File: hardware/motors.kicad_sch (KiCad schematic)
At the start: 11 parts, among them J2 JST_PH_01x02, J3 JST_XH_01x02, J4 JST_XH_01x02, U3 DRV8212, U4 DRV8212

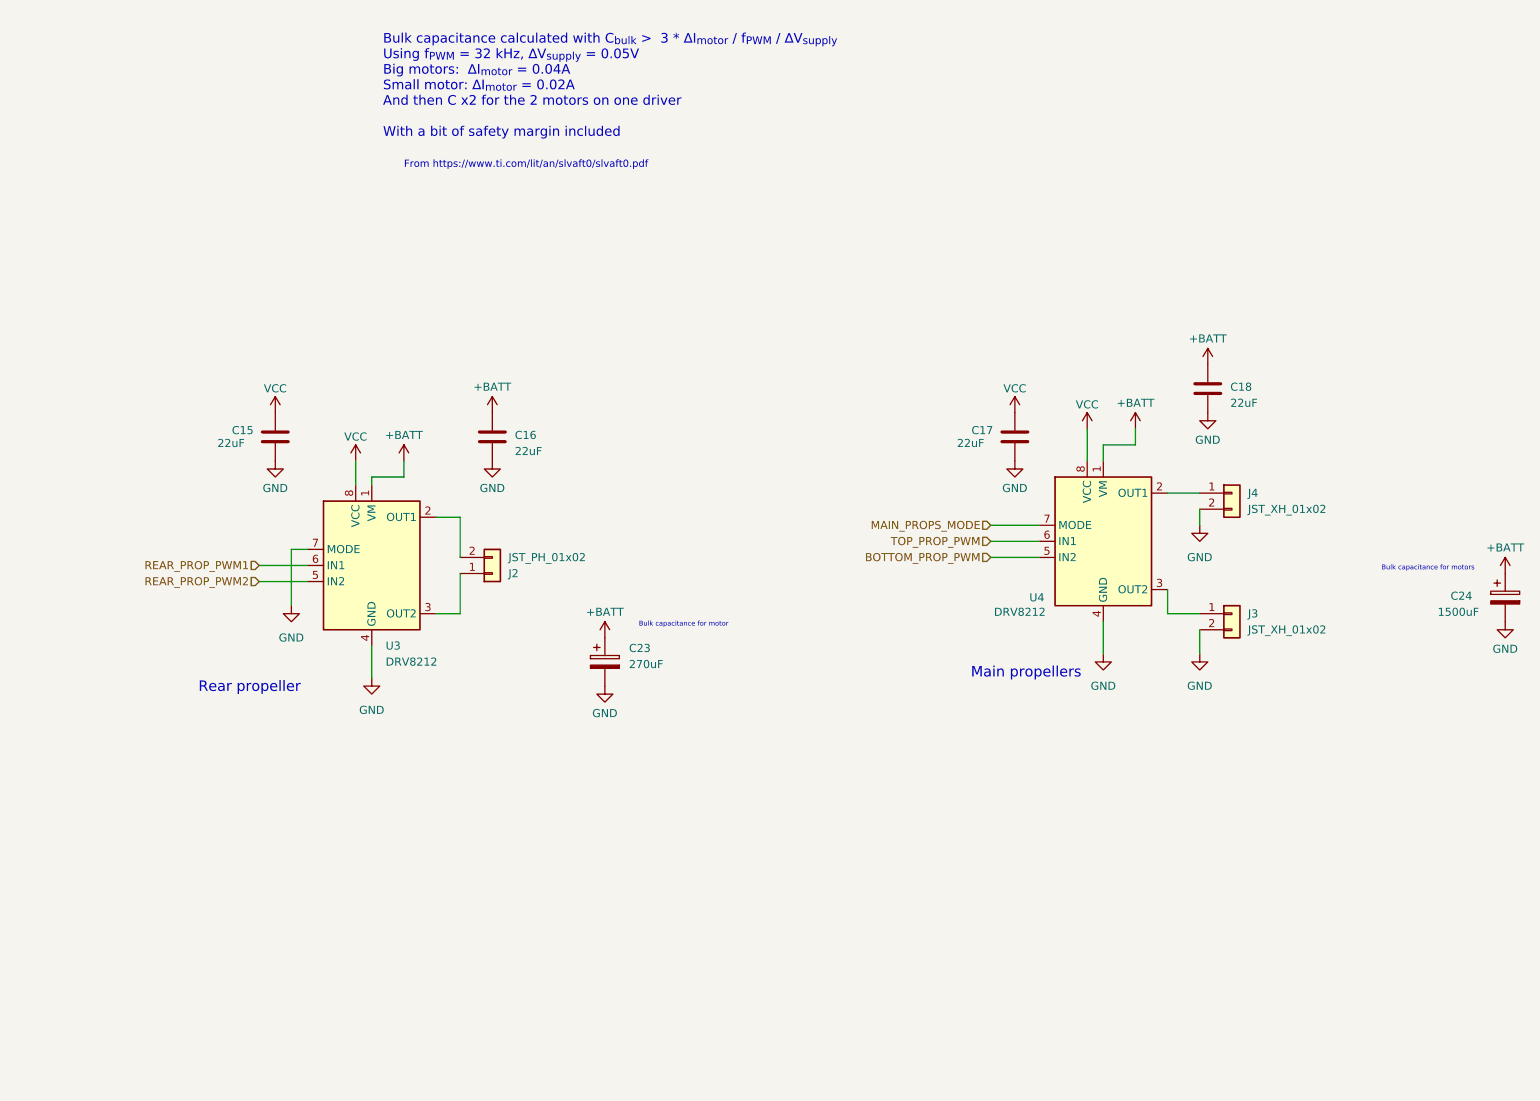
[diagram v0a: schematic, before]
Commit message: Experiment to see if 3rd motor driver is possible
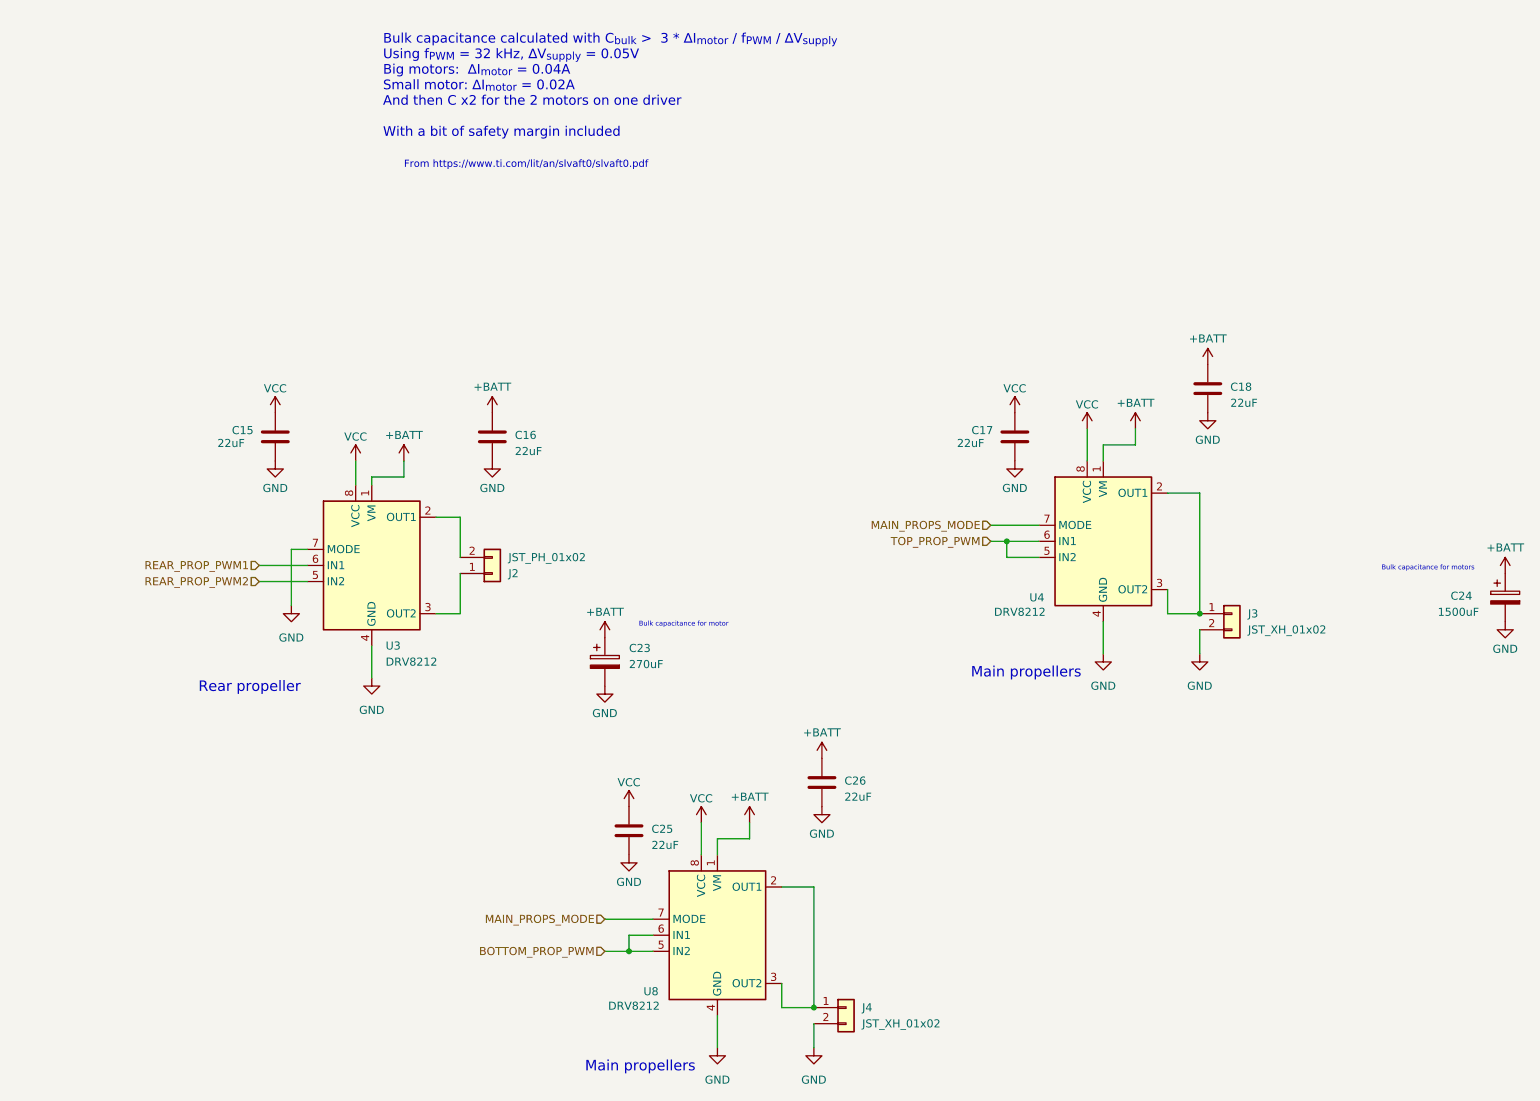
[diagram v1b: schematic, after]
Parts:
- added C25, C26: 22uF, Capacitor_SMD:C_0603_1608Metric_Pad1.08x0.95mm_HandSolder, symbol Device:C
- added U8: DRV8212, heli-footprints:WSON-8-1EP_2x2mm_P0.5mm_EP0.9x1.6mm_ThermalVias, symbol heli_symbols:DRV8212
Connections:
- net +BATT: now also C26.1, U8.1 (VM)
- net BOTTOM_PROP_PWM: now also U8.5 (IN2), U8.6 (IN1); no longer U4.5 (IN2)
- net GND: now also C25.2, C26.2, U8.4 (GND), U8.9 (GND)
- net MAIN_PROPS_MODE: now also U8.7 (MODE)
- net TOP_PROP_PWM: now also U4.5 (IN2)
- net VCC: now also C25.1, U8.8 (VCC)
- net at J4.1 (Pin_1): now also U8.2 (OUT1), U8.3 (OUT2); no longer U4.2 (OUT1)
- net at J3.1 (Pin_1), U4.3 (OUT2): now also U4.2 (OUT1)

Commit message: Finalise schematic to include 3rd motor driver
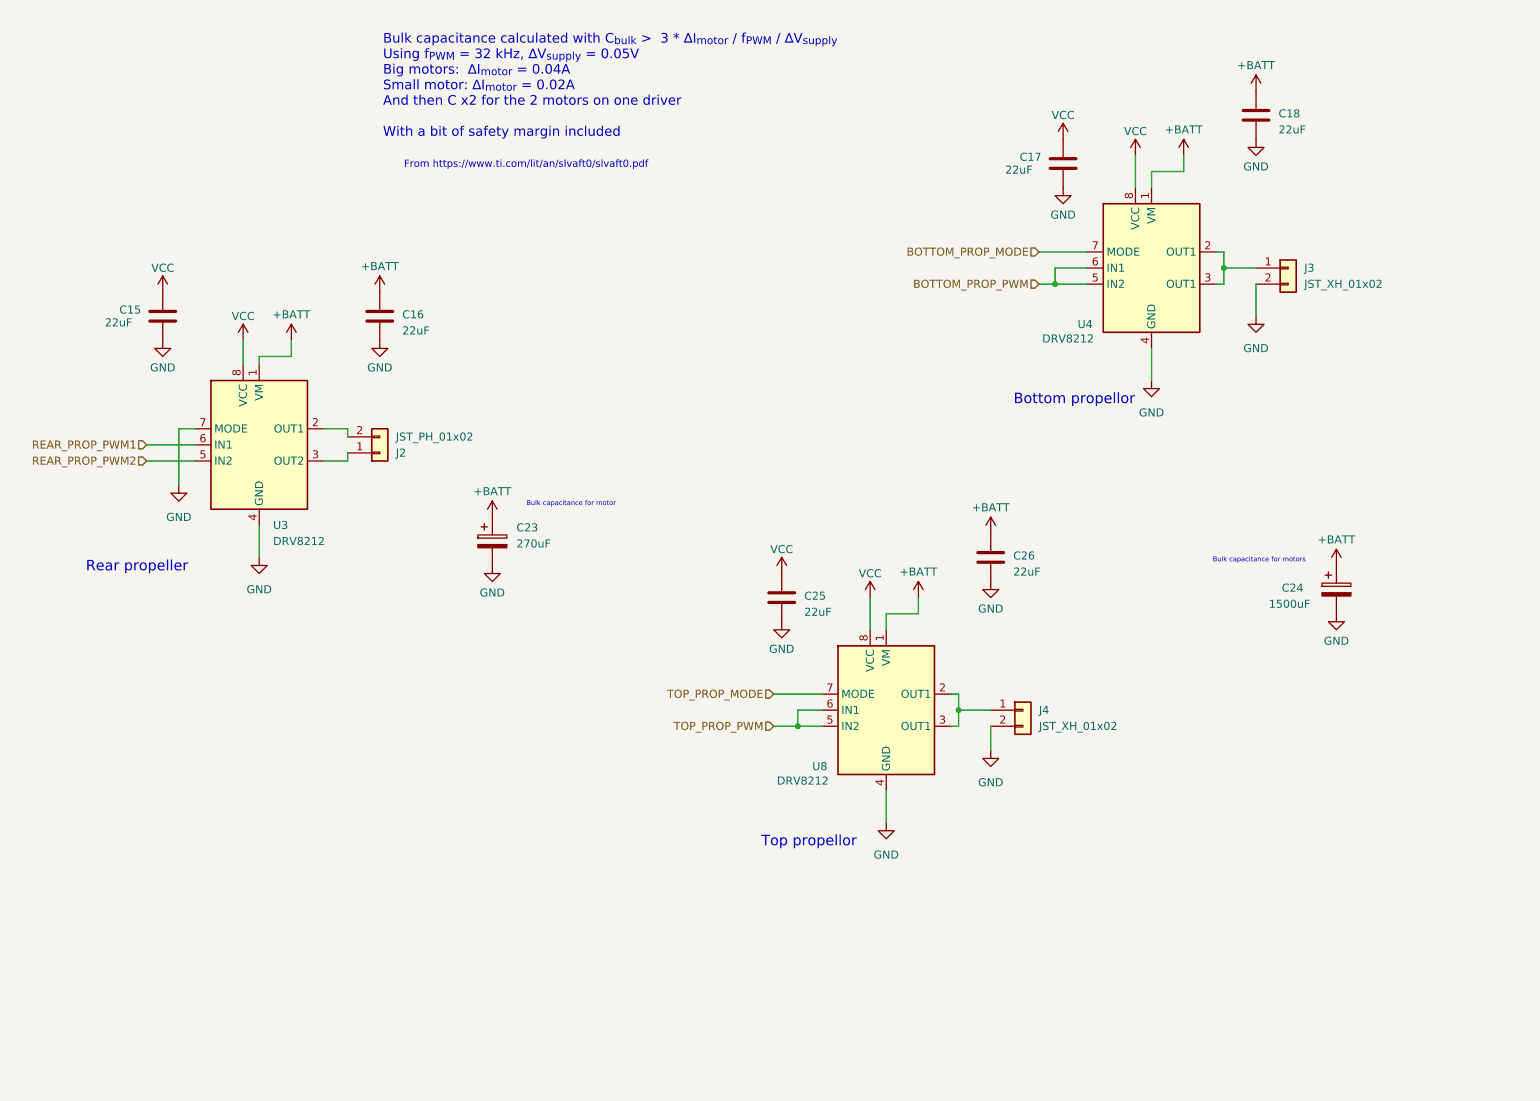
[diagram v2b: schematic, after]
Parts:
- U3, U4, U8: footprint heli-footprints:WSON-8-1EP_2x2mm_P0.5mm_EP0.9x1.6mm_ThermalVias -> Package_SON:WSON-8-1EP_2x2mm_P0.5mm_EP0.9x1.6mm_ThermalVias
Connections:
- net BOTTOM_PROP_PWM: now also U4.5 (IN2), U4.6 (IN1); no longer U8.5 (IN2), U8.6 (IN1)
- net TOP_PROP_PWM: now also U8.5 (IN2), U8.6 (IN1); no longer U4.5 (IN2), U4.6 (IN1)
- net MAIN_PROPS_MODE renamed BOTTOM_PROP_MODE
- net BOTTOM_PROP_MODE: no longer U8.7 (MODE)
- new net TOP_PROP_MODE: U8.7 (MODE)
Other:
- note added: "Bottom propellor"
- note added: "Top propellor"
- note removed: "Main propellers"
- moved on the sheet: C15, C16, C17, C18, C23, C24, C25, C26, J2, J3, J4, U3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

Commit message: Correct pin ordering for 3rd motor driver
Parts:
- U3, U4, U8: footprint Package_SON:WSON-8-1EP_2x2mm_P0.5mm_EP0.9x1.6mm_ThermalVias -> heli-footprints:WSON-8-1EP_2x2mm_P0.5mm_EP0.9x1.6mm_ThermalVias
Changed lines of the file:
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@@
 			)
 		)
-		(property "Footprint" "Package_SON:WSON-8-1EP_2x2mm_P0.5mm_EP0.9x1.6mm_ThermalVias"
+		(property "Footprint" "heli-footprints:WSON-8-1EP_2x2mm_P0.5mm_EP0.9x1.6mm_ThermalVias"
 			(at 157.48 152.4 0)
 			(effects
@@
 			)
 		)
-		(property "Footprint" "Package_SON:WSON-8-1EP_2x2mm_P0.5mm_EP0.9x1.6mm_ThermalVias"
+		(property "Footprint" "heli-footprints:WSON-8-1EP_2x2mm_P0.5mm_EP0.9x1.6mm_ThermalVias"
 			(at 199.39 82.55 0)
 			(effects
@@
 			)
 		)
-		(property "Footprint" "Package_SON:WSON-8-1EP_2x2mm_P0.5mm_EP0.9x1.6mm_ThermalVias"
+		(property "Footprint" "heli-footprints:WSON-8-1EP_2x2mm_P0.5mm_EP0.9x1.6mm_ThermalVias"
 			(at 58.42 110.49 0)
 			(effects

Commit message: Added part numbers for ~1/2 of components
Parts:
- C15, C16, C17, C18, C25, C26: LCSC Part # (none) -> C59461; MPN (none) -> CL10A226MQ8NRNC
- C23: value 270uF -> 1000uF; LCSC Part # (none) -> C3024245; MPN (none) -> SPT1AM102E14ORVZC
- C24: value 1500uF -> 3300uF; LCSC Part # (none) -> C240437; MPN (none) -> RL1A332MG250A00CE0
- U3, U4, U8: LCSC Part # (none) -> C2843766; MPN (none) -> DRV8212DSGR
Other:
- note added: "Bulk capacitance for main motors"
- note added: "Bulk capacitance for tail motor"
- note added: "Minimum bulk capacitance calculated with C_{bulk} > 3 * ∆I_{motor} / f_{PWM} / ∆V_{supply} Using f_{PWM} = 32 kHz, ∆V_{supply} = 0.05V Big motors: ∆I_{motor} = 0.04A Small motor: ∆I_{motor} = 0.02A And then C x2 for the 2 motors on one driver With a bit of safety margin included. Then just went up to the maximum value I could find on LCSC for the diameters that would fit on the pcb."
- note removed: "Bulk capacitance calculated with C_{bulk} > 3 * ∆I_{motor} / f_{PWM} / ∆V_{supply} Using f_{PWM} = 32 kHz, ∆V_{supply} = 0.05V Big motors: ∆I_{motor} = 0.04A Small motor: ∆I_{motor} = 0.02A And then C x2 for the 2 motors on one driver With a bit of safety margin included"
- note removed: "Bulk capacitance for motor"
- note removed: "Bulk capacitance for motors"

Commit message: Updates to fields for PCBWay BOM generation
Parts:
- C23, C24, J2, J3, J4: now left out of the parts list
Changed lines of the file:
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@@
 		(unit 1)
 		(exclude_from_sim no)
-		(in_bom yes)
+		(in_bom no)
 		(on_board yes)
 		(dnp no)
@@
 		(unit 1)
 		(exclude_from_sim no)
-		(in_bom yes)
+		(in_bom no)
 		(on_board yes)
 		(dnp no)
@@
 		(unit 1)
 		(exclude_from_sim no)
-		(in_bom yes)
+		(in_bom no)
 		(on_board yes)
 		(dnp no)
@@
 		(unit 1)
 		(exclude_from_sim no)
-		(in_bom yes)
+		(in_bom no)
 		(on_board yes)
 		(dnp no)
@@
 		(unit 1)
 		(exclude_from_sim no)
-		(in_bom yes)
-		(on_board yes)
-		(dnp no)
+		(in_bom no)
+		(on_board yes)
+		(dnp no)
